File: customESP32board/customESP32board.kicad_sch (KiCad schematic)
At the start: 50 parts, among them J1 USB_B, J2 Conn_01x16_Pin, J3 Conn_01x16_Pin, Q1 S8050, Q2 S8050, Q3 BSS138, Q4 BSS138, Q5 BSS138, SW1 SW_Push, SW2 SW_Push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

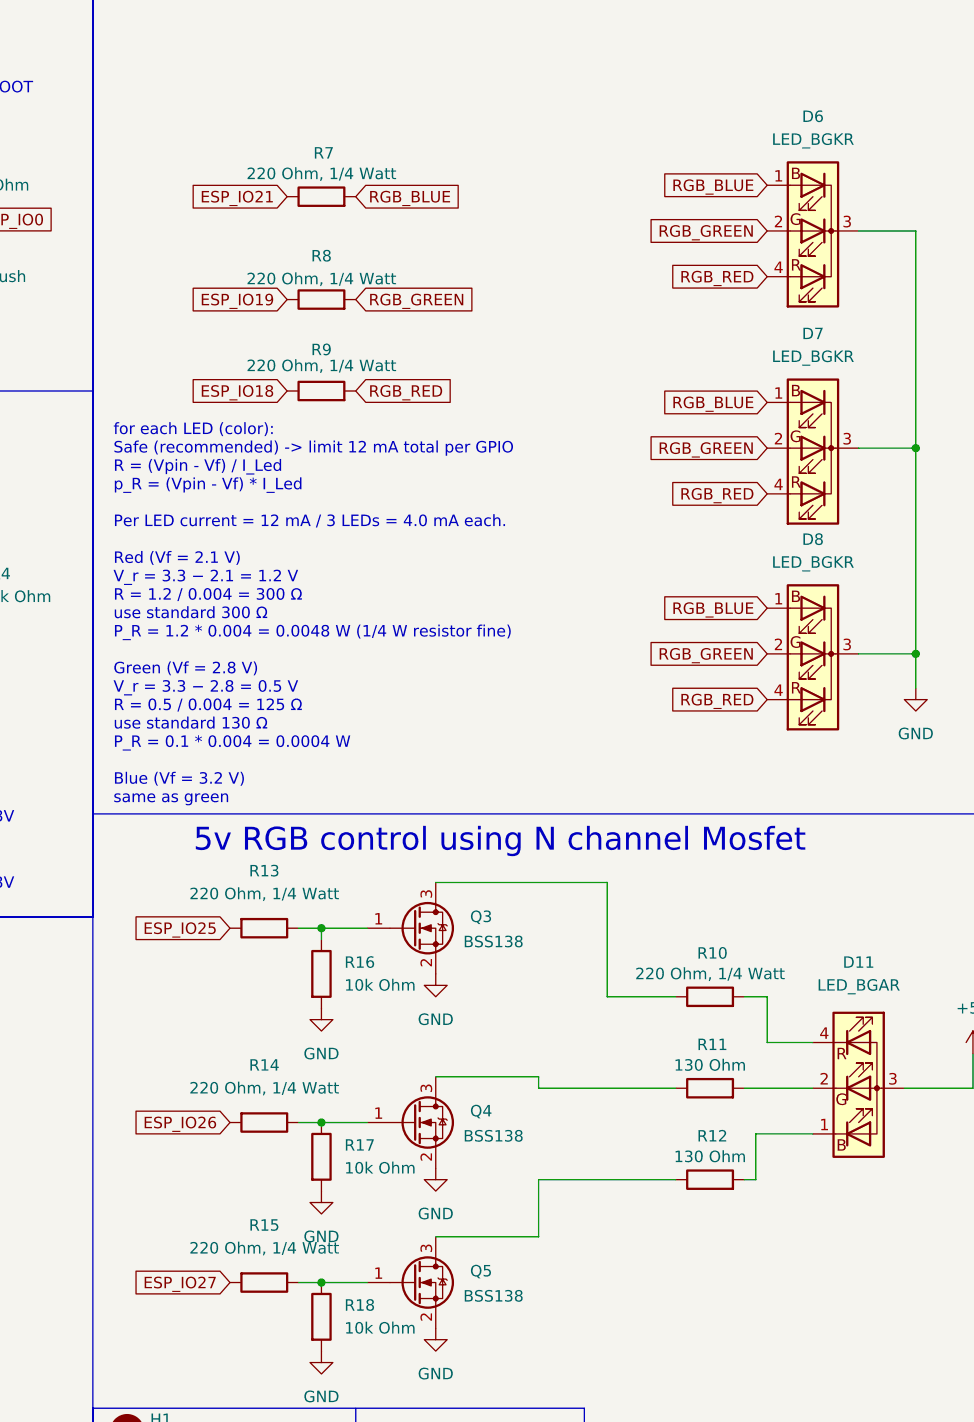
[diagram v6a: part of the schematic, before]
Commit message: updated resistance 220 Ohm with 0603 footprint to 200 Ohm beacuse its obselete in uge electronics
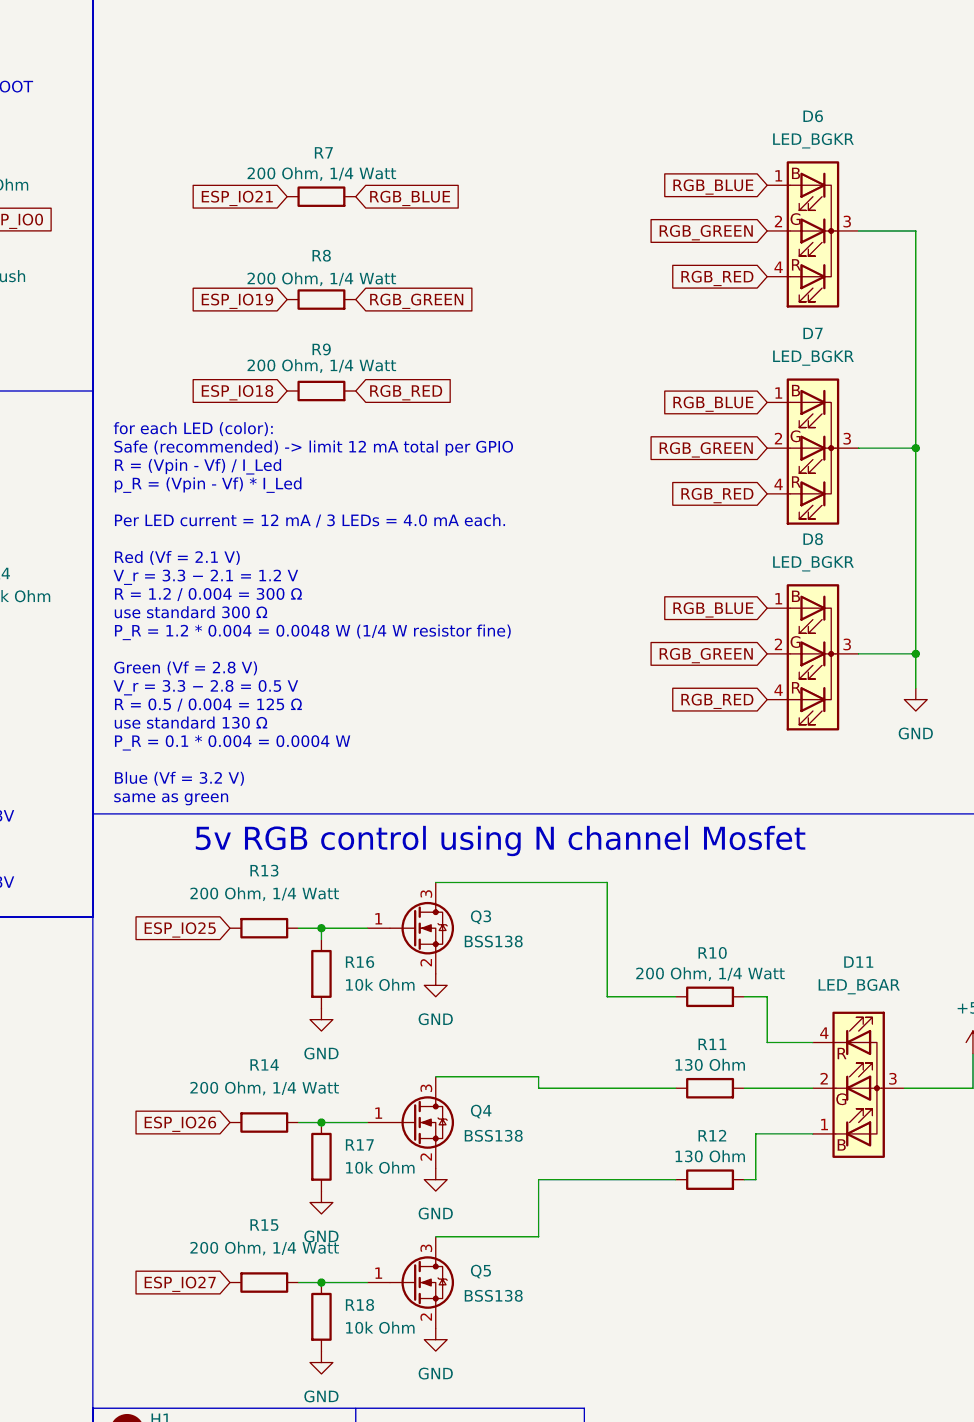
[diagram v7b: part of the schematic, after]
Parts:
- R10, R13, R14, R15, R7, R8, R9: value 220 Ohm, 1/4 Watt -> 200 Ohm, 1/4 Watt
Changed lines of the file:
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@@
 			)
 		)
-		(property "Value" "220 Ohm, 1/4 Watt"
+		(property "Value" "200 Ohm, 1/4 Watt"
 			(at 140.97 118.11 90)
 			(effects
@@
 			)
 		)
-		(property "Value" "220 Ohm, 1/4 Watt"
+		(property "Value" "200 Ohm, 1/4 Watt"
 			(at 147.32 59.436 90)
 			(effects
@@
 			)
 		)
-		(property "Value" "220 Ohm, 1/4 Watt"
+		(property "Value" "200 Ohm, 1/4 Watt"
 			(at 190.5 127 90)
 			(effects
@@
 			)
 		)
-		(property "Value" "220 Ohm, 1/4 Watt"
+		(property "Value" "200 Ohm, 1/4 Watt"
 			(at 147.32 38.1 90)
 			(effects
@@
 			)
 		)
-		(property "Value" "220 Ohm, 1/4 Watt"
+		(property "Value" "200 Ohm, 1/4 Watt"
 			(at 140.97 139.7 90)
 			(effects
@@
 			)
 		)
-		(property "Value" "220 Ohm, 1/4 Watt"
+		(property "Value" "200 Ohm, 1/4 Watt"
 			(at 140.97 157.48 90)
 			(effects
@@
 			)
 		)
-		(property "Value" "220 Ohm, 1/4 Watt"
+		(property "Value" "200 Ohm, 1/4 Watt"
 			(at 147.32 49.784 90)
 			(effects

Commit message: updated schematic
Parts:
- C1, C7: footprint Capacitor_SMD:C_0805_2012Metric -> Capacitor_SMD:C_1206_3216Metric_Pad1.33x1.80mm_HandSolder
- C11: footprint Capacitor_SMD:C_1206_3216Metric -> Capacitor_SMD:C_1206_3216Metric_Pad1.33x1.80mm_HandSolder
- C3, C6: footprint Capacitor_SMD:C_0603_1608Metric -> Capacitor_SMD:C_1206_3216Metric_Pad1.33x1.80mm_HandSolder
- D2, D3, D4: footprint Diode_SMD:D_SOD-323 -> Diode_SMD:D_SOD-323_HandSoldering
- D5, D9: footprint LED_SMD:LED_0603_1608Metric -> LED_SMD:LED_1206_3216Metric_Pad1.42x1.75mm_HandSolder
- H1, H2: footprint MountingHole:MountingHole_2.2mm_M2_Pad_Via -> MountingHole:MountingHole_3.2mm_M3_Pad_Via
- R1, R11, R12, R16, R17, R18, R2, R3: footprint Resistor_SMD:R_0805_2012Metric -> Resistor_SMD:R_1206_3216Metric_Pad1.30x1.75mm_HandSolder
- R10, R13, R14, R15, R9: value 200 Ohm, 1/4 Watt -> 200 Ohm; footprint Resistor_SMD:R_0603_1608Metric -> Resistor_SMD:R_1206_3216Metric_Pad1.30x1.75mm_HandSolder
- R4: footprint Resistor_SMD:R_0603_1608Metric -> Resistor_SMD:R_1206_3216Metric_Pad1.30x1.75mm_HandSolder
- R5, R6: value 10 Ohm -> 10k Ohm; footprint Resistor_SMD:R_1206_3216Metric -> Resistor_SMD:R_1206_3216Metric_Pad1.30x1.75mm_HandSolder
- R7, R8: value 200 Ohm, 1/4 Watt -> 130 Ohm; footprint Resistor_SMD:R_0603_1608Metric -> Resistor_SMD:R_1206_3216Metric_Pad1.30x1.75mm_HandSolder
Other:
- moved on the sheet: D6, D7, D8, R5, R6, R7, R8, R9, SW1, SW2
